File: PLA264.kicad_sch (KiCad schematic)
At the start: 9 parts, among them J1 PLA_Socket, U1 GAL16V8

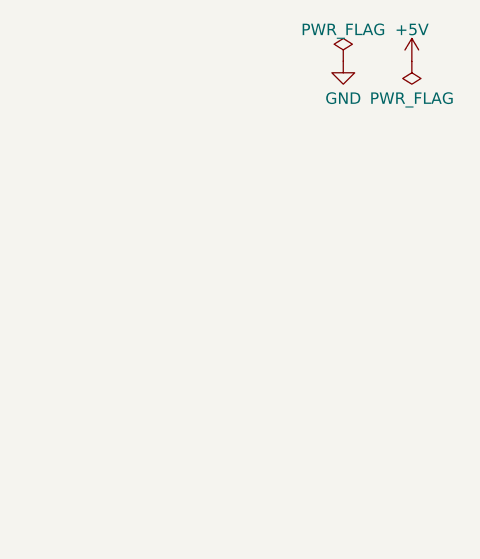
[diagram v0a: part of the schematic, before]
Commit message: Revised layout.
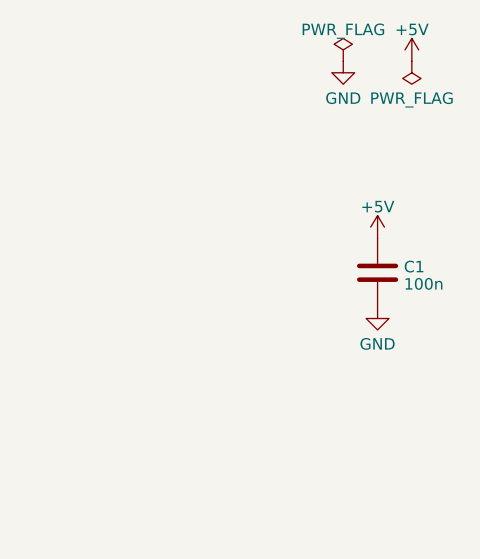
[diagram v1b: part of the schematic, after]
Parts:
- added C1: 100n, Capacitor_SMD:C_0603_1608Metric, symbol Device:C
- D1, D2, D3, D4, D5, D6: footprint Diode_SMD:D_0603_1608Metric -> Diode_SMD:D_SOD-323
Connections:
- net +5V: now also C1.1
- net GND: now also C1.2
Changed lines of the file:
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@@
       (effects (font (size 1.27 1.27)))
     )
-    (property "Footprint" "Diode_SMD:D_0603_1608Metric" (at 97.79 41.91 90)
+    (property "Footprint" "Diode_SMD:D_SOD-323" (at 97.79 41.91 90)
       (effects (font (size 1.27 1.27)) hide)
     )
@@
       (effects (font (size 1.27 1.27)))
     )
-    (property "Footprint" "Diode_SMD:D_0603_1608Metric" (at 160.02 52.07 90)
+    (property "Footprint" "Diode_SMD:D_SOD-323" (at 160.02 52.07 90)
       (effects (font (size 1.27 1.27)) hide)
     )
@@
     )
   )
+  (symbol (lib_id "power:GND") (at 262.255 53.975 0) (unit 1)
+    (in_bom yes) (on_board yes) (dnp no) (fields_autoplaced)
+    (property "Reference" "#PWR07" (at 262.255 60.325 0)
+      (effects (font (size 1.27 1.27)) hide)
+    )
+    (property "Value" "GND" (at 262.255 58.1105 0)
+      (effects (font (size 1.27 1.27)))
+    )
+    (property "Footprint" "" (at 262.255 53.975 0)
+      (effects (font (size 1.27 1.27)) hide)
+    )
+    (property "Datasheet" "" (at 262.255 53.975 0)
+      (effects (font (size 1.27 1.27)) hide)
+    )
+    (pin "1")
+    (instances
+      (project "PLA264"
+        (path "/4116a878-e864-4c30-8d07-a7d0a94f3434"
+          (reference "#PWR07") (unit 1)
+        )
+      )
+    )
+  )
+  (symbol (lib_id "Device:C") (at 262.255 50.165 0) (unit 1)
+    (in_bom yes) (on_board yes) (dnp no) (fields_autoplaced)
+    (property "Reference" "C1" (at 265.176 49.5213 0)
+      (effects (font (size 1.27 1.27)) (justify left))
+    )
+    (property "Value" "100n" (at 265.176 51.4423 0)
+      (effects (font (size 1.27 1.27)) (justify left))
+    )
+    (property "Footprint" "Capacitor_SMD:C_0603_1608Metric" (at 263.2202 53.975 0)
+      (effects (font (size 1.27 1.27)) hide)
+    )
+    (property "Datasheet" "~" (at 262.255 50.165 0)
+      (effects (font (size 1.27 1.27)) hide)
+    )
+    (pin "1")
+    (pin "2")
+    (instances
+      (project "PLA264"
+        (path "/4116a878-e864-4c30-8d07-a7d0a94f3434"
+          (reference "C1") (unit 1)
+        )
+      )
+    )
+  )
   (symbol (lib_id "Device:D_Small") (at 160.02 54.61 0) (unit 1)
     (in_bom yes) (on_board yes) (dnp no) (fields_autoplaced)
@@
       (effects (font (size 1.27 1.27)))
     )
-    (property "Footprint" "Diode_SMD:D_0603_1608Metric" (at 160.02 54.61 90)
+    (property "Footprint" "Diode_SMD:D_SOD-323" (at 160.02 54.61 90)
       (effects (font (size 1.27 1.27)) hide)
     )
@@
       (effects (font (size 1.27 1.27)))
     )
-    (property "Footprint" "Diode_SMD:D_0603_1608Metric" (at 97.79 54.61 90)
+    (property "Footprint" "Diode_SMD:D_SOD-323" (at 97.79 54.61 90)
       (effects (font (size 1.27 1.27)) hide)
     )
@@
       (effects (font (size 1.27 1.27)))
     )
-    (property "Footprint" "Diode_SMD:D_0603_1608Metric" (at 160.02 57.15 90)
+    (property "Footprint" "Diode_SMD:D_SOD-323" (at 160.02 57.15 90)
       (effects (font (size 1.27 1.27)) hide)
     )
@@
       (effects (font (size 1.27 1.27)))
     )
-    (property "Footprint" "Diode_SMD:D_0603_1608Metric" (at 160.02 44.45 90)
+    (property "Footprint" "Diode_SMD:D_SOD-323" (at 160.02 44.45 90)
       (effects (font (size 1.27 1.27)) hide)
     )
@@
         )
       )
+    )
+  )
+  (symbol (lib_id "power:+5V") (at 262.255 46.355 0) (unit 1)
+    (in_bom yes) (on_board yes) (dnp no) (fields_autoplaced)
+    (property "Reference" "#PWR08" (at 262.255 50.165 0)
+      (effects (font (size 1.27 1.27)) hide)
+    )
+    (property "Value" "+5V" (at 262.255 42.8531 0)
+      (effects (font (size 1.27 1.27)))
+    )
+    (property "Footprint" "" (at 262.255 46.355 0)
+      (effects (font (size 1.27 1.27)) hide)
+    )
+    (property "Datasheet" "" (at 262.255 46.355 0)
+      (effects (font (size 1.27 1.27)) hide)
+    )
+    (pin "1")
+    (instances
+      (project "PLA264"
+        (path "/4116a878-e864-4c30-8d07-a7d0a94f3434"
+          (reference "#PWR08") (unit 1)
+        )
+      )

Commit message: Cleaning up.
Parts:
- D1: renamed from D5; value D_Small -> 1N4148WS
- D2: renamed from D6; value D_Small -> 1N4148WS
- D3: renamed from D1; value D_Small -> 1N4148WS
- D4: renamed from D2; value D_Small -> 1N4148WS
- D5: renamed from D3; value D_Small -> 1N4148WS
- D6: renamed from D4; value D_Small -> 1N4148WS
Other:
- company: (none) -> www.hackup.net
- title: (none) -> PLA264
- moved on the sheet: D1, D2, R1, U1

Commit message: Preparing for Gerber export.
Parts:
- C1: LCSC (none) -> C14663
- D1, D2, D3, D4, D5, D6: LCSC (none) -> C2128
- R1: value R -> 5k6; LCSC (none) -> C23189
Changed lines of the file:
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@@
+      (effects (font (size 1.27 1.27)) hide)
+    )
+    (property "LCSC" "C2128" (at 104.14 41.91 0)
       (effects (font (size 1.27 1.27)) hide)
     )
@@
     )
     (property "Sim.Pins" "1=K 2=A" (at 160.02 52.07 0)
+      (effects (font (size 1.27 1.27)) hide)
+    )
+    (property "LCSC" "C2128" (at 160.02 52.07 0)
       (effects (font (size 1.27 1.27)) hide)
     )
@@
       (effects (font (size 1.27 1.27)) hide)
     )
+    (property "LCSC" "C14663" (at 262.255 50.165 0)
+      (effects (font (size 1.27 1.27)) hide)
+    )
     (pin "1")
     (pin "2")
@@
       (effects (font (size 1.27 1.27)) hide)
     )
+    (property "LCSC" "C2128" (at 160.02 54.61 0)
+      (effects (font (size 1.27 1.27)) hide)
+    )
     (pin "1")
     (pin "2")
@@
       (effects (font (size 1.27 1.27)) hide)
     )
+    (property "LCSC" "C2128" (at 104.14 54.61 0)
+      (effects (font (size 1.27 1.27)) hide)
+    )
     (pin "1")
     (pin "2")
@@
       (effects (font (size 1.27 1.27)) hide)
     )
+    (property "LCSC" "C2128" (at 160.02 57.15 0)
+      (effects (font (size 1.27 1.27)) hide)
+    )
     (pin "1")
     (pin "2")
@@
     )
     (property "Sim.Pins" "1=K 2=A" (at 160.02 44.45 0)
+      (effects (font (size 1.27 1.27)) hide)
+    )
+    (property "LCSC" "C2128" (at 160.02 44.45 0)
       (effects (font (size 1.27 1.27)) hide)
     )
@@
       (effects (font (size 1.27 1.27)) (justify left))
     )
-    (property "Value" "R" (at 124.333 116.2123 0)
+    (property "Value" "5k6" (at 124.333 116.2123 0)
       (effects (font (size 1.27 1.27)) (justify left))
     )
@@
       (effects (font (size 1.27 1.27)) hide)
     )
+    (property "LCSC" "C23189" (at 122.555 114.935 0)
+      (effects (font (size 1.27 1.27)) hide)
+    )
